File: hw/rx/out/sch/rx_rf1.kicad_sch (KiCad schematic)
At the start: 9 parts, among them J3 ANT_A, J4 ANT_B, J5 TO_MODULE, U2 PE4259

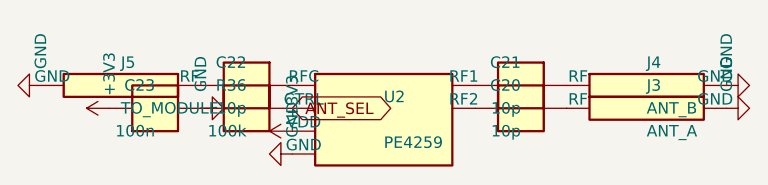
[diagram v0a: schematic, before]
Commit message: hw/rx: review fixes for #81 (mute relay + supervisor, S1J clamps, VCM discharge + 2-pole filter, 16 V LDOs, keyed header, I2S DNP, cable stability + power-cycle SPICE, FLT low latency) (#32)
Co-Authored-By: Claude Opus 5.5 <noreply@anthropic.com>
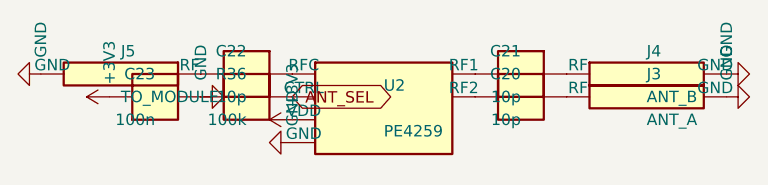
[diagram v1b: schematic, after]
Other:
- moved on the sheet: C20, C21, C22, C23, J3, J4, J5, R36, U2
